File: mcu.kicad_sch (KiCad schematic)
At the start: 23 parts, among them J1 USB4105-GF-A-120, U1 STM32G473CEUx, Y1 ECS-240-6-37B-7KM-TR

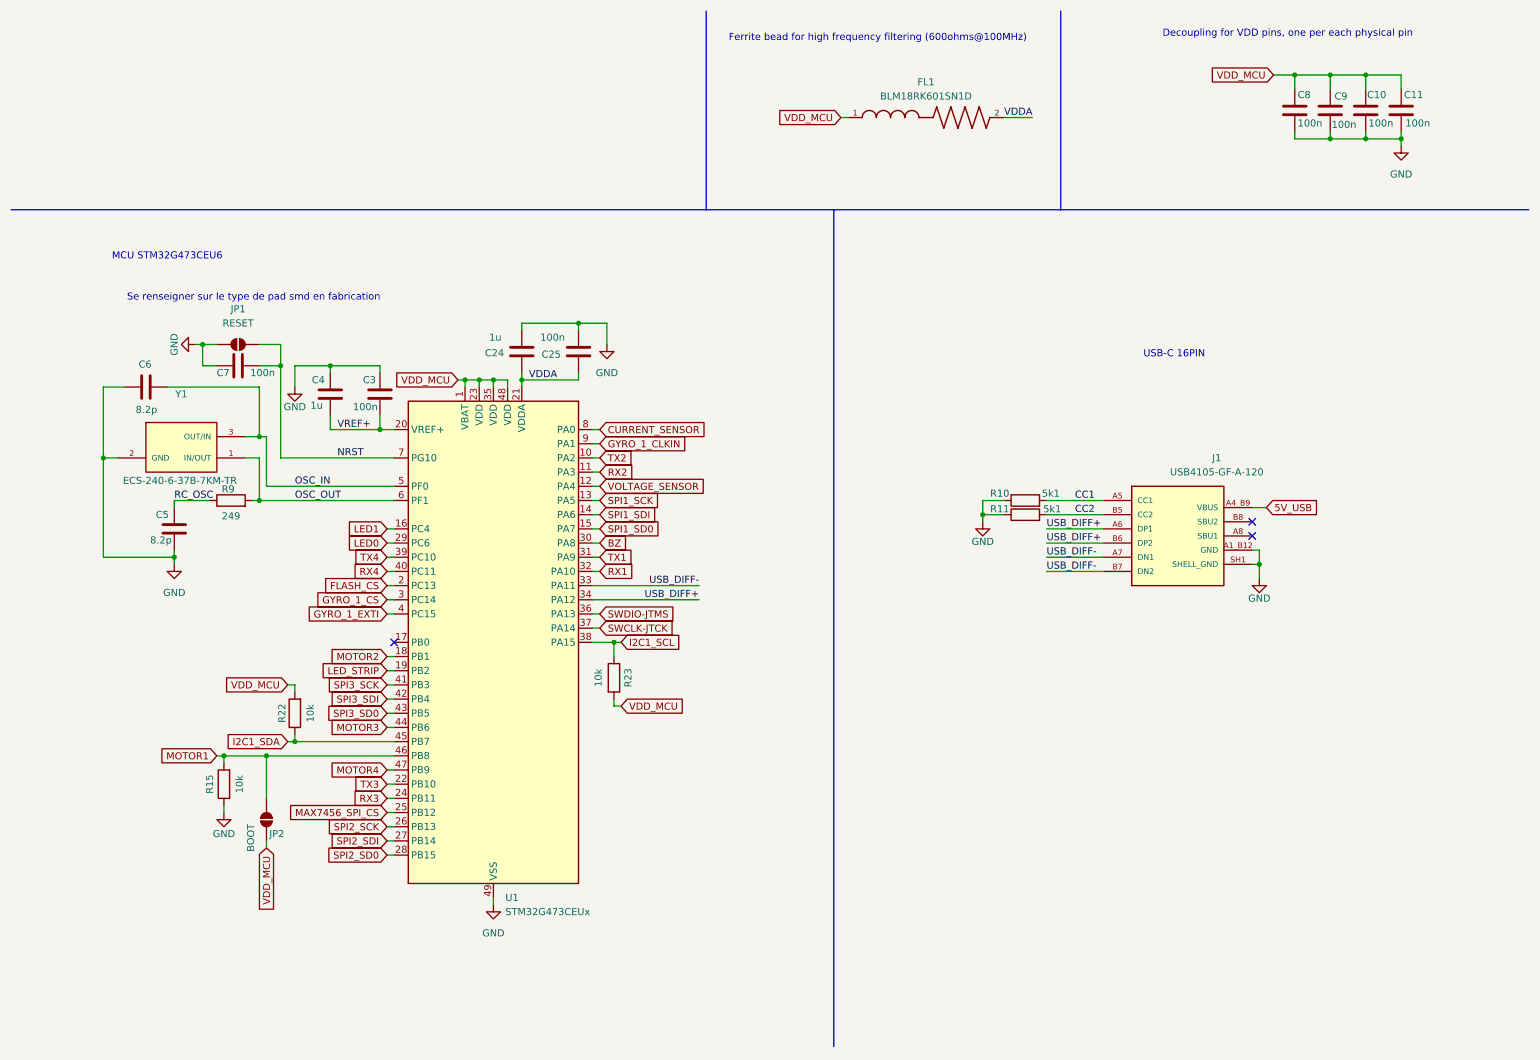
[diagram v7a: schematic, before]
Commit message: switch stm323g473ceu6 to stm32g473cet6 for easier soldering package
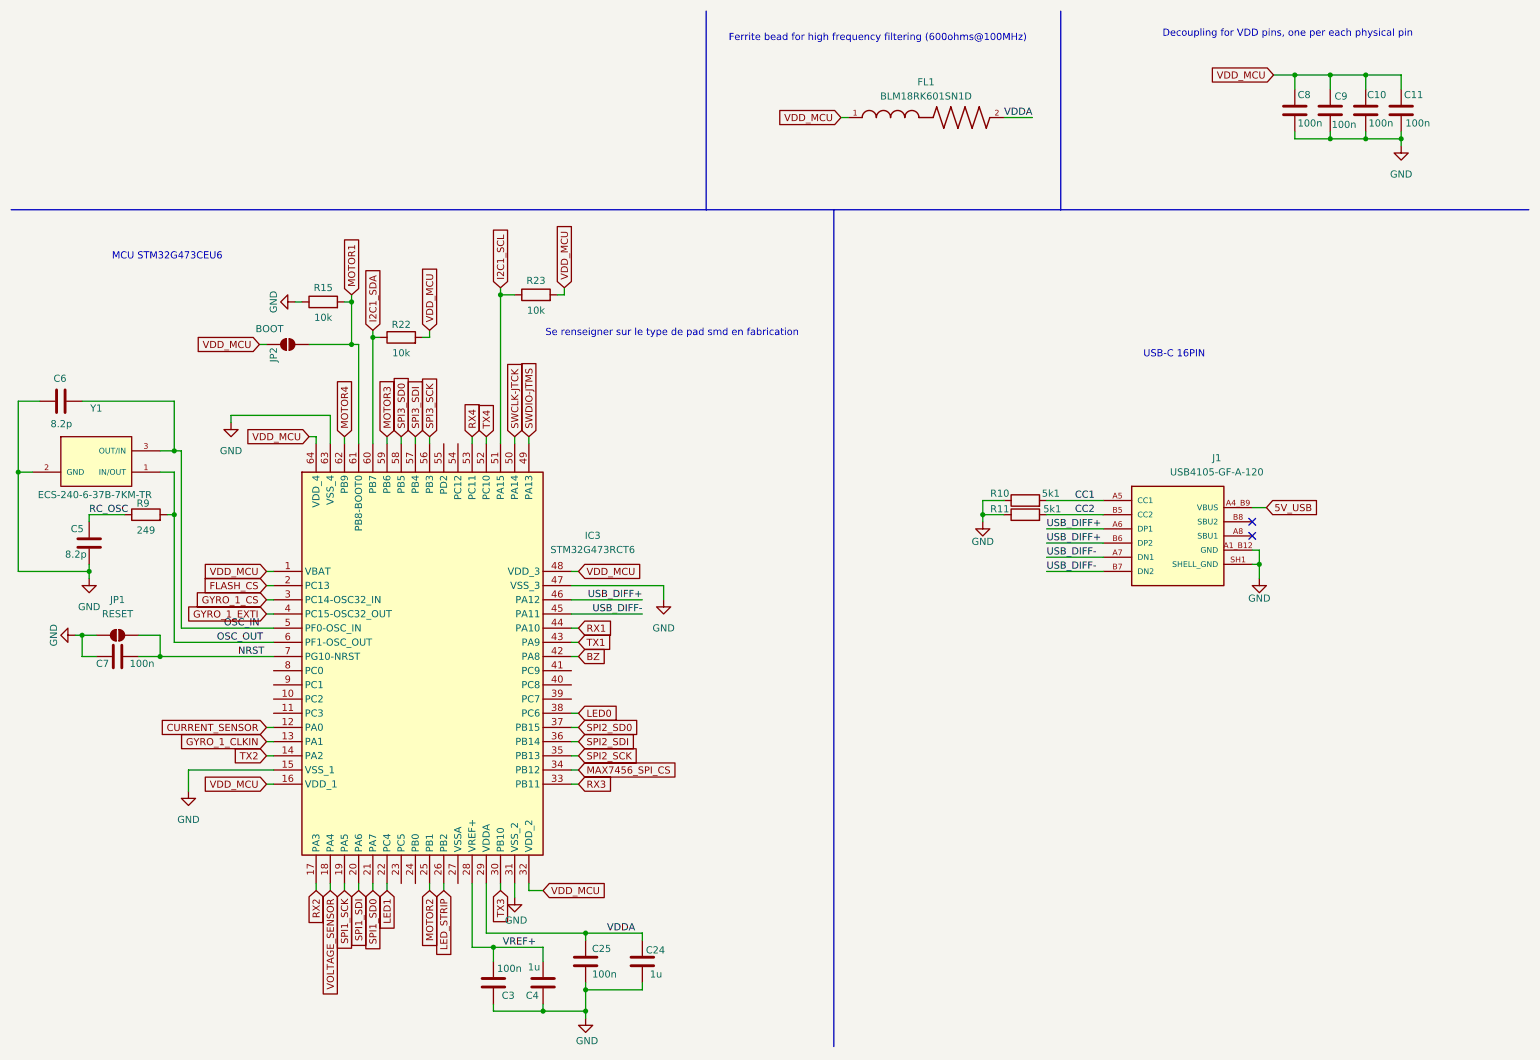
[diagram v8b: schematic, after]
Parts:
- removed U1: STM32G473CEUx, fcg4_fp:QFN-48-1EP_7x7mm_P0.5mm_EP5.6x5.6mm, symbol MCU_ST_STM32G4:STM32G473CEUx
- added IC3: STM32G473RCT6, fcg4_fp:QFP50P1200X1200X160-64M, symbol fcg4:STM32G473RCT6
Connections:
- net BZ: now also IC3.42 (PA8)
- net CURRENT_SENSOR: now also IC3.12 (PA0)
- net FLASH_CS: now also IC3.2 (PC13)
- net GND: now also IC3.15 (VSS_1), IC3.31 (VSS_2), IC3.47 (VSS_3), IC3.63 (VSS_4)
- net GYRO_1_CLKIN: now also IC3.13 (PA1)
- net GYRO_1_CS: now also IC3.3 (PC14-OSC32_IN)
- net GYRO_1_EXTI: now also IC3.4 (PC15-OSC32_OUT)
- net I2C1_SCL: now also IC3.51 (PA15)
- net I2C1_SDA: now also IC3.60 (PB7)
- net LED0: now also IC3.38 (PC6)
- net LED1: now also IC3.22 (PC4)
- net LED_STRIP: now also IC3.26 (PB2)
- net MAX7456_SPI_CS: now also IC3.34 (PB12)
- net MOTOR1: now also IC3.61 (PB8-BOOT0)
- net MOTOR2: now also IC3.25 (PB1)
- net MOTOR3: now also IC3.59 (PB6)
- net MOTOR4: now also IC3.62 (PB9)
- net NRST: now also IC3.7 (PG10-NRST)
- net OSC_IN: now also IC3.5 (PF0-OSC_IN)
- net OSC_OUT: now also IC3.6 (PF1-OSC_OUT)
- net RX1: now also IC3.44 (PA10)
- net RX2: now also IC3.17 (PA3)
- net RX3: now also IC3.33 (PB11)
- net RX4: now also IC3.53 (PC11)
- net SPI1_SCK: now also IC3.19 (PA5)
- net SPI1_SD0: now also IC3.21 (PA7)
- net SPI1_SDI: now also IC3.20 (PA6)
- net SPI2_SCK: now also IC3.35 (PB13)
- net SPI2_SD0: now also IC3.37 (PB15)
- net SPI2_SDI: now also IC3.36 (PB14)
- net SPI3_SCK: now also IC3.56 (PB3)
- net SPI3_SD0: now also IC3.58 (PB5)
- net SPI3_SDI: now also IC3.57 (PB4)
- net SWCLK-JTCK: now also IC3.50 (PA14)
- net SWDIO-JTMS: now also IC3.49 (PA13)
- net TX1: now also IC3.43 (PA9)
- net TX2: now also IC3.14 (PA2)
- net TX3: now also IC3.30 (PB10)
- net TX4: now also IC3.52 (PC10)
- net USB_DIFF+: now also IC3.46 (PA12)
- net USB_DIFF-: now also IC3.45 (PA11)
- net VDDA: now also IC3.29 (VDDA)
- net VDD_MCU: now also IC3.1 (VBAT), IC3.16 (VDD_1), IC3.32 (VDD_2), IC3.48 (VDD_3), IC3.64 (VDD_4)
- net VOLTAGE_SENSOR: now also IC3.18 (PA4)
- net VREF+: now also IC3.28 (VREF+)
- no-connect marks 3 -> 2
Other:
- moved on the sheet: C24, C25, C3, C4, C5, C6, C7, JP1, JP2, R15, R22, R23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
